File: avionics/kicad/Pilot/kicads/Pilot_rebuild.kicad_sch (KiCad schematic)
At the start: 8 parts

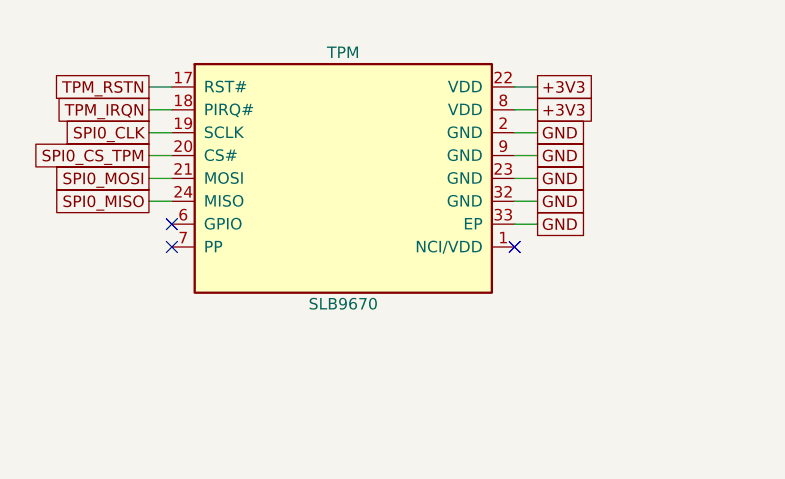
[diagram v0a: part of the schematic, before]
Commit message: Migrate fleet TPM from Infineon SLB9670 to SLB9672
Replaces every active reference to the SLB9670 TPM with SLB9672 across
KiCad symbols/schematics/PCBs/netlists, generator scripts, firmware
device-tree overlays, and documentation (REFERENCES.md, WBS/TODO,
current-specification, graphical build guide). Archived files, frozen
revision snapshots, and the old datasheet PDF are left untouched.

- Added avionics/datasheets/SLB_9672XU20_Infineon.pdf (Infineon DS Rev
  1.3, 2024-11-18) and a new clean-room symbol/pinmap
  (Observer_SLB9672_TPM.kicad_sym, SLB9672XU2_0_pinmap.csv), replacing
  the superseded SLB9670 symbol/pinmap.
- Verified the physical footprint is unchanged (5x5mm body, 0.5mm
  pitch, 32-pin QFN, 3.6x3.6mm exposed pad per both datasheets), so the
  existing Package_DFN_QFN:QFN-32-1EP_5x5mm_P0.5mm_EP3.45x3.45mm
  footprint was reused as-is. Pin *functions* do differ (SLB9672 makes
  pins 1/14/22 the mandatory VDD pins vs 8/22 on SLB9670; pin 6 is now a
  true no-connect instead of GPIO; pins 3/4/7 are GPIO_00/01/02 instead
  of NCI/NCI/PP) -- the new symbol and every net-map/pinmap that lists
  pin functions reflect the corrected pinout.
- Populated the corrected component into Observer, Commo, Flight
  Engineer, and CAN-PERIPH-GW-1's schematics (lib_symbol block +
  instances) and into every board's PCB Value/property text. Pilot's
  and XO's own independently-authored inline TPM symbols were text-
  renamed only, preserving their pre-existing (and separately tracked)
  wrong-pin-number defect -- out of scope for this swap.
- Firmware: infineon,slb9670 -> infineon,slb9672 compatible string and
  tpm_slb9670: -> tpm_slb9672: node label in both active cape DTS
  overlays.
- REFERENCES.md REF-SENSOR-011 updated in place with validated Infineon
  URLs; new open items logged for (a) re-running kicad-cli ERC/DRC
  (unavailable in this environment) and (b) a newly-found, unrelated
  pre-existing footprint-mismatch defect on XO's placed TPM.
- PROJECT_INDEX.md / t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
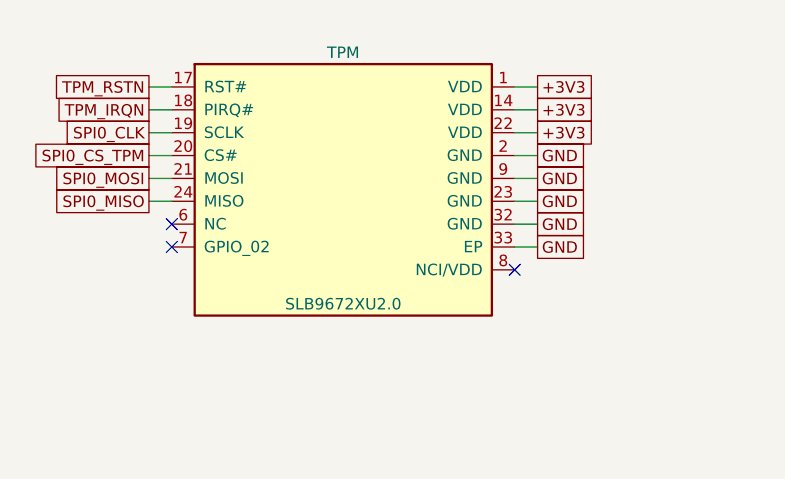
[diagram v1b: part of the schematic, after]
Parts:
- TPM: value SLB9670 -> SLB9672XU2.0
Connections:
- net +3V3: now also TPM.1 (VDD), TPM.14 (VDD); no longer TPM.8 (VDD)
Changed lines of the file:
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@@
     (exclude_from_sim no) (in_bom yes) (on_board yes) (dnp no)
     (property "Reference" "TPM" (at 279.40 62.23 0) (effects (font (size 1.27 1.27))))
-    (property "Value" "SLB9670" (at 279.40 90.17 0) (effects (font (size 1.27 1.27))))
+    (property "Value" "SLB9672XU2.0" (at 279.40 90.17 0) (effects (font (size 1.27 1.27))))
     (pin "17")
     (pin "18")
@@
     (pin "33")
     (pin "1")
+    (pin "14")
     (instances (project "Pilot" (path "/a3000000-0000-0000-0000-000000000001" (reference "TPM") (unit 1))))
   )
@@
   (global_label "+3V3" (shape passive) (at 300.99 68.58 0) (effects (font (size 1.27 1.27)) (justify left)))
   (wire (pts (xy 298.45 71.12) (xy 300.99 71.12)) (stroke (width 0) (type default)))
-  (global_label "GND" (shape passive) (at 300.99 71.12 0) (effects (font (size 1.27 1.27)) (justify left)))
+  (global_label "+3V3" (shape passive) (at 300.99 71.12 0) (effects (font (size 1.27 1.27)) (justify left)))
   (wire (pts (xy 298.45 73.66) (xy 300.99 73.66)) (stroke (width 0) (type default)))
   (global_label "GND" (shape passive) (at 300.99 73.66 0) (effects (font (size 1.27 1.27)) (justify left)))
@@
   (wire (pts (xy 298.45 81.28) (xy 300.99 81.28)) (stroke (width 0) (type default)))
   (global_label "GND" (shape passive) (at 300.99 81.28 0) (effects (font (size 1.27 1.27)) (justify left)))
-  (no_connect (at 298.45 83.82))
+  (wire (pts (xy 298.45 83.82) (xy 300.99 83.82)) (stroke (width 0) (type default)))
+  (global_label "GND" (shape passive) (at 300.99 83.82 0) (effects (font (size 1.27 1.27)) (justify left)))
+  (no_connect (at 298.45 86.36))
   (symbol (lib_id "S_GPS") (at 76.20 228.60 0) (unit 1)
     (exclude_from_sim no) (in_bom yes) (on_board yes) (dnp no)
